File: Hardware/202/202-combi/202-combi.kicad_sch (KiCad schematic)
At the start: 36 parts, among them J1 DM3CS-SF, P3 LEFT-201, P4 RIGHT-201, P8 202-SMART-CAM-P, U1 TXS0104, U2 TXS0104, U3 ASE-24.000MHZ-LC-T2, U5 TCA9534PWR, U6 TPS79628DCQ

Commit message: Added MSP430
This will be the only expander in the future. Experiment for now
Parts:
- added U4: Smart_Cam_Expander_MSP430FR2355, Ziloo:MSP430FR2355TRSMR, symbol Ziloo:Smart_Cam_Expander_MSP430FR2355
- C1, C2: value (none) -> 1uF
- C11, C17, C3, C4, C5: value (none) -> 100nF
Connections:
- net +1V8: now also U4.5 (DVCC)
- net GND: now also U4.6 (DVSS)
- net LEFT_ATT_INT: now also U4.28 (P3-2_OA2-)
- net LEFT_ATT_XSHUT: now also U4.27 (P3-3_OA2+)
- net LEFT_PWRDN: now also U4.30 (P3-0_MCLK)
- net LEFT_RESET: now also U4.29 (P3-1_OA2O)
- net RIGHT_ATT_INT: now also U4.24 (P3-6_OA3-)
- net RIGHT_ATT_XSHUT: now also U4.23 (P3-7_OA3+)
- net RIGHT_PWRDN: now also U4.26 (P3-4_SMCLK)
- net RIGHT_RESET: now also U4.25 (P3-5_OA3O)
- net at J1.1 (DAT2), P8.51 (SD_D2): now also R5.1; no longer R8.1
- net at J1.2 (CD/DAT3), P8.49 (SD_D3): now also R6.1; no longer R7.1
- net at J1.3 (CMD), P8.59 (SD_CMD): now also R7.1; no longer R6.1
- net at J1.5 (CLK), P8.57 (SD_CLK): now also R8.1; no longer R9.1
- net at J1.7 (DAT0), P8.55 (SD_D0): now also R9.1; no longer R10.1
- net at J1.8 (DAT1), P8.53 (SD_D1): now also R10.1; no longer R5.1
- net STEM_SCL: now reaches P8.36 (STEM_SCL)
- net STEM_SDA: now reaches P8.38 (STEM_SDA)
- net STEM_INT: now reaches P8.40 (STEM_INT)
- net SYS_SCL renamed SYS_SCL_1V8
- net SYS_SCL_1V8: now also U4.11 (P4-7_SYS_SCL)
- net SYS_SDA renamed SYS_SDA_1V8
- net SYS_SDA_1V8: now also U4.12 (P4-6_SYS_SDA)
- new net MCU_SYS_INT_1V8: U4.15 (P4-1_MCU_SYS_INT)
- new net STEM_INT_1V8: U4.16 (P4-0_STEM_INT)
- new net STEM_SCL_1V8: U4.31 (P1-3_STEM_SCL_OA0+_A3)
- new net STEM_SDA_1V8: U4.32 (P1-2_STEM_SDA_TB0TRG_OA0-_A2_Veref-)
- no-connect marks 17 -> 14
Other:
- note added: "This is experiemental for now, unfinished connection"
- moved on the sheet: C1, C11, C17, C18, C19, C2, C20, C21, C3, C4, C5, C6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

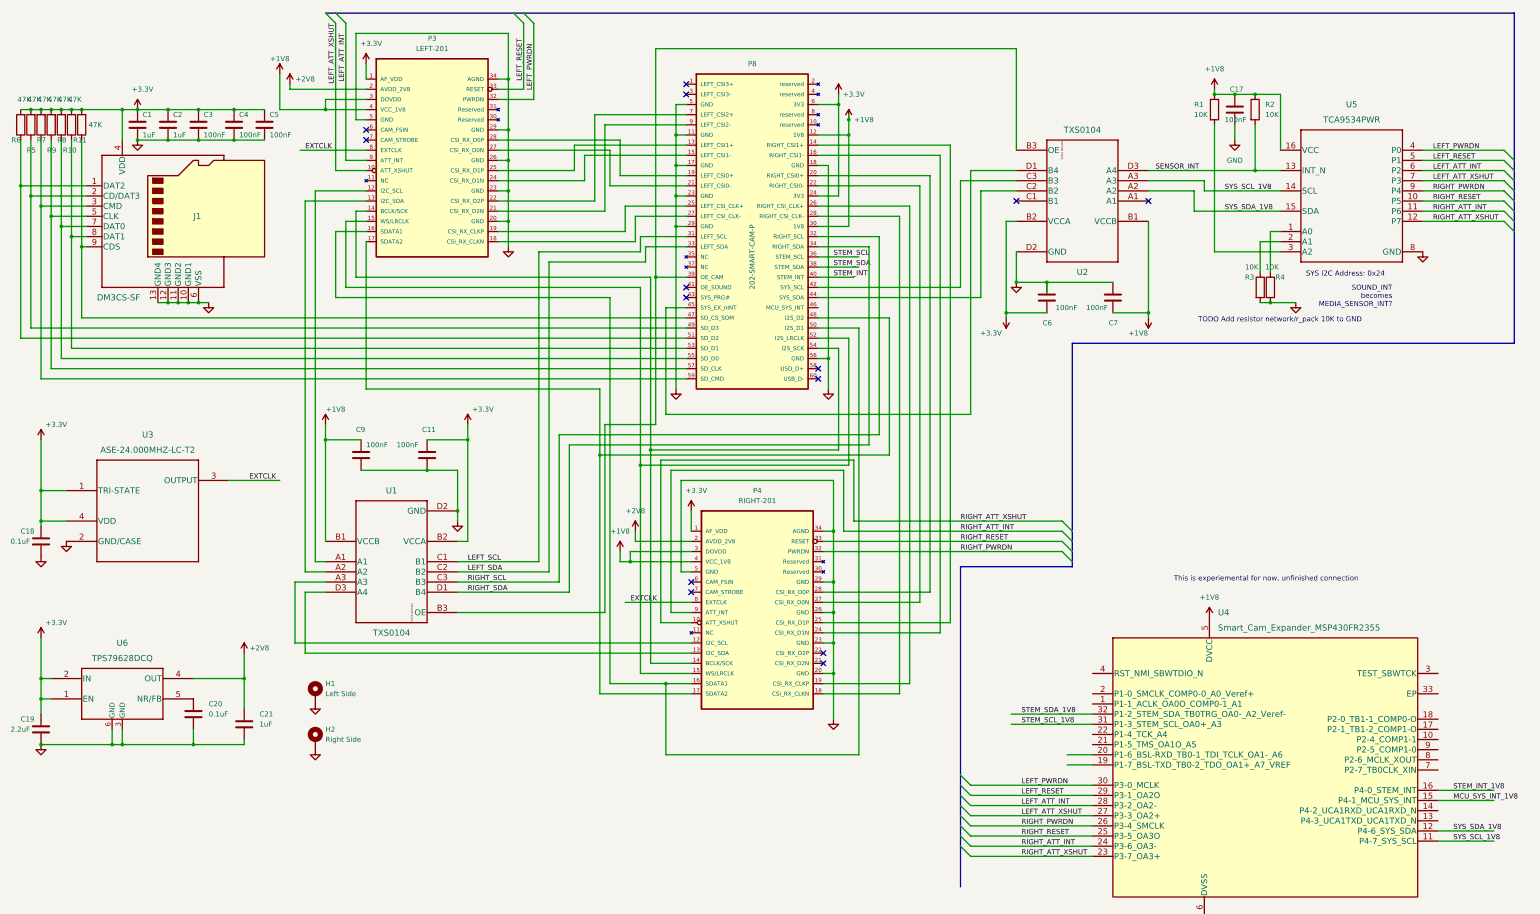
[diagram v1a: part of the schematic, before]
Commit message: Schematic clean-up
-Cleaned-up shcematics
-Added a TVS diode array to the SDCard connector.
-Impedances are calculated
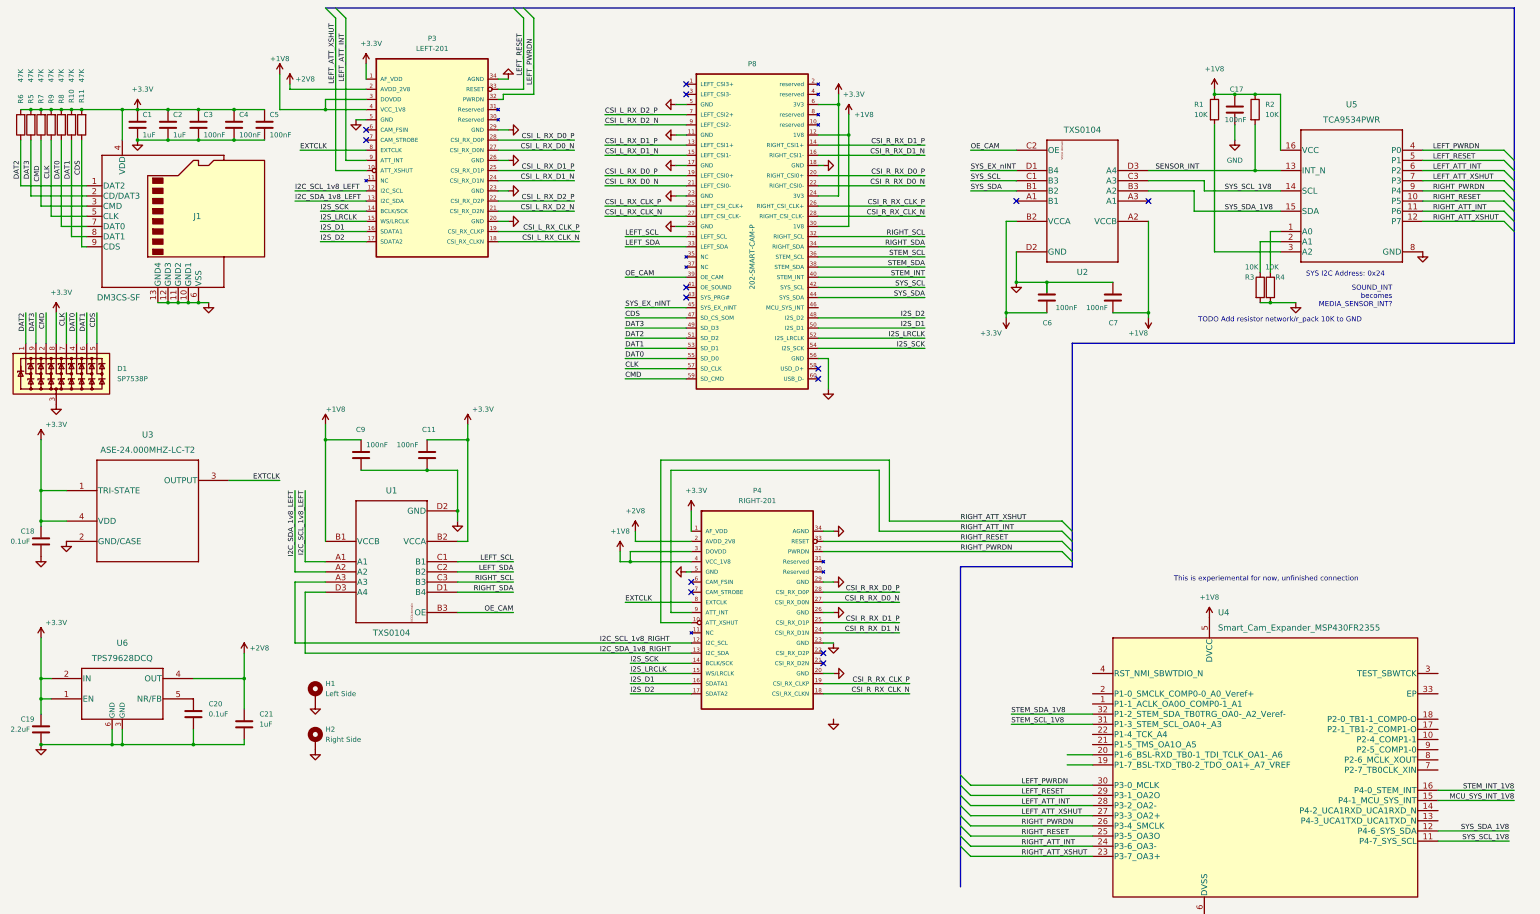
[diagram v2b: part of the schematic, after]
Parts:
- added D1: SP7538P, Package_DFN_QFN:UDFN-9_1.0x3.8mm_P0.5mm, symbol Ziloo:SP7538P
- U1: Supplier Link (none) -> https://www.digikey.com/en/products/detail/texas-instrument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
- U2: symbol Ziloo:TXS0104EYZTR -> Ziloo:TXS0104EYZTR_corrected; Supplier Link (none) -> https://www.digikey.com/en/products/detail/texas-instrument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
- U4: Supplier Link (none) -> https://eu.mouser.com/ProductDetail/Texas-Instruments/MSP43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
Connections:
- net +1V8: now also U2.A2 (VCCB); no longer U2.B1 (VCCB)
- net +3.3V: now also D1.8 (K7)
- net GND: now also D1.3 (A); no longer P4.20 (GND)
- net SYS_SCL_1V8: now also U2.C3 (A3); no longer U2.A3
- net SYS_SDA_1V8: now also U2.B3 (A2); no longer U2.A2
- net DAT2: now reaches J1.1 (DAT2), P8.51 (SD_D2), R5.1
- net DAT2: now also D1.1 (K1)
- net DAT3: now reaches J1.2 (CD/DAT3), P8.49 (SD_D3), R6.1
- net DAT3: now also D1.9 (K8)
- net CMD: now reaches J1.3 (CMD), P8.59 (SD_CMD), R7.1
- net CMD: now also D1.2 (K2)
- net CLK: now reaches J1.5 (CLK), P8.57 (SD_CLK), R8.1
- net CLK: now also D1.7 (K6)
- net DAT0: now reaches J1.7 (DAT0), P8.55 (SD_D0), R9.1
- net DAT0: now also D1.4 (K3)
- net DAT1: now reaches J1.8 (DAT1), P8.53 (SD_D1), R10.1
- net DAT1: now also D1.6 (K5)
- net CDS: now reaches J1.9 (CDS), P8.47 (SD_CS_SOM), R11.1
- net CDS: now also D1.5 (K4)
- net OE_CAM: now reaches P8.39 (OE_CAM), U1.B3 (OE)
- net OE_CAM: now also U2.C2 (OE); no longer U2.B3 (OE)
- net SYS_SCL: now reaches U2.C1 (B3)
- net SYS_SCL: now also P8.42 (SYS_SCL)
- net SYS_SDA: now reaches P8.44 (SYS_SDA)
- net SYS_SDA: now also U2.B1 (B2); no longer U2.C2 (B2)
- net SYS_EX_nINT: now reaches P8.45 (SYS_EX_nINT), U2.D1 (B4)
- net I2C_SCL_1v8_LEFT: now reaches P3.12 (I2C_SCL), U1.A1
- net I2C_SDA_1v8_LEFT: now reaches P3.13 (I2C_SDA), U1.A2
- net I2S_SCK: now reaches P3.14 (BCLK/SCK), P4.14 (BCLK/SCK), P8.54 (I2S_SCK)
- net I2S_LRCLK: now reaches P3.15 (WS/LRCLK), P4.15 (WS/LRCLK), P8.52 (I2S_LRCLK)
- net I2S_D1: now reaches P3.16 (SDATA1), P4.16 (SDATA1), P8.50 (I2S_D1)
- net I2S_D2: now reaches P3.17 (SDATA2), P4.17 (SDATA2), P8.48 (I2S_D2)
- net CSI_L_RX_CLK_N: now reaches P3.18 (CSI_RX_CLKN), P8.27 (LEFT_CSI_CLK-)
- net CSI_L_RX_CLK_P: now reaches P3.19 (CSI_RX_CLKP), P8.25 (LEFT_CSI_CLK+)
- net CSI_L_RX_D2_N: now reaches P3.21 (CSI_RX_D2N), P8.9 (LEFT_CSI2-)
- net CSI_L_RX_D2_P: now reaches P3.22 (CSI_RX_D2P), P8.7 (LEFT_CSI2+)
- net CSI_L_RX_D1_N: now reaches P3.24 (CSI_RX_D1N), P8.15 (LEFT_CSI1-)
- net CSI_L_RX_D1_P: now reaches P3.25 (CSI_RX_D1P), P8.13 (LEFT_CSI1+)
- net CSI_L_RX_D0_N: now reaches P3.27 (CSI_RX_D0N), P8.21 (LEFT_CSI0-)
- net CSI_L_RX_D0_P: now reaches P3.28 (CSI_RX_D0P), P8.19 (LEFT_CSI0+)
- net CSI_R_RX_D1_P: now reaches P4.25 (CSI_RX_D1P), P8.14 (RIGHT_CSI1+)
- net CSI_R_RX_D1_N: now reaches P4.24 (CSI_RX_D1N), P8.16 (RIGHT_CSI1-)
- net CSI_R_RX_D0_P: now reaches P4.28 (CSI_RX_D0P), P8.20 (RIGHT_CSI0+)
- net CSI_R_RX_D0_N: now reaches P4.27 (CSI_RX_D0N), P8.22 (RIGHT_CSI0-)
- net CSI_R_RX_CLK_P: now reaches P4.19 (CSI_RX_CLKP), P8.26 (RIGHT_CSI_CLK+)
- net CSI_R_RX_CLK_N: now reaches P4.18 (CSI_RX_CLKN), P8.28 (RIGHT_CSI_CLK-)
- net I2C_SCL_1v8_RIGHT: now reaches P4.12 (I2C_SCL), U1.A3
- net I2C_SDA_1v8_RIGHT: now reaches P4.13 (I2C_SDA), U1.D3 (A4)
